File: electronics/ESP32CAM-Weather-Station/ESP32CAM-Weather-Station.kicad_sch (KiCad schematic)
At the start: 93 parts, among them IC1 BME688, IC2 SGP41-D-R4, IC3 VEML7700-TT, IC4 BQ24093DGQR, IC5 BQ29707DSET, IC6 MCP3426A0T-E_SN, IC7 TPS63070RNMR, J1 B4B-PH-SM4-TB_LF__SN_, J10 Conn_01x02_Pin, J2 B4B-PH-SM4-TB_LF__SN_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

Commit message: [WIP] Placed basic 3v3 regulator parts.
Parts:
- Q2: footprint CSD16406Q3:DQG_VSON-CLIP -> DQG_VSON-CLIP
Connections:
- net +3.3V: no longer C5.1
- net +VBAT: no longer S1.1 (NO_1), U2.5 (EN)
- net at Q2.5 (D_1), Q2.6 (D_2), Q2.7 (D_3)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: now also Q2.9 (D_EP), Q3.9 (D_EP)
- net 3V3_PREFUSE: now reaches F2.2, U2.1 (VOUT)
- net 3V3_PREFUSE: now also C5.1
- new net REG_EN: S1.1 (NO_1), U2.5 (EN)
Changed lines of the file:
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@@
 	)
 	(junction
-		(at 349.25 26.67)
-		(diameter 0)
-		(color 0 0 0 0)
-	)
-	(junction
 		(at 40.64 189.23)
 		(diameter 0)
@@
 	)
 	(junction
-		(at 379.73 26.67)
+		(at 137.16 68.58)
 		(diameter 0)
 		(color 0 0 0 0)
 	)
 	(junction
-		(at 137.16 68.58)
+		(at 45.72 142.24)
 		(diameter 0)
 		(color 0 0 0 0)
@@
 	)
 	(junction
+		(at 59.69 58.42)
+		(diameter 0)
+		(color 0 0 0 0)
+	)
+	(junction
 		(at 341.63 241.3)
 		(diameter 0)
@@
 	(wire
 		(pts
+			(xy 59.69 58.42) (xy 72.39 58.42)
+		)
+		(stroke
+			(width 0)
+			(type default)
+		)
+	)
+	(wire
+		(pts
 			(xy 143.51 68.58) (xy 148.59 68.58)
 		)
@@
 	(wire
 		(pts
+			(xy 46.99 58.42) (xy 59.69 58.42)
+		)
+		(stroke
+			(width 0)
+			(type default)
+		)
+	)
+	(wire
+		(pts
 			(xy 341.63 233.68) (xy 347.98 233.68)
 		)
@@
 	(wire
 		(pts
-			(xy 349.25 26.67) (xy 349.25 22.86)
+			(xy 110.49 134.62) (xy 110.49 147.32)
 		)
 		(stroke
@@
 	(wire
 		(pts
-			(xy 349.25 22.86) (xy 379.73 22.86)
+			(xy 71.12 86.36) (xy 76.2 86.36)
 		)
 		(stroke
@@
 	(wire
 		(pts
-			(xy 71.12 86.36) (xy 76.2 86.36)
+			(xy 358.14 236.22) (xy 369.57 236.22)
 		)
 		(stroke
@@
 	(wire
 		(pts
-			(xy 358.14 236.22) (xy 369.57 236.22)
+			(xy 382.27 194.31) (xy 392.43 194.31)
 		)
 		(stroke
@@
 	(wire
 		(pts
-			(xy 382.27 194.31) (xy 392.43 194.31)
+			(xy 45.72 133.35) (xy 45.72 142.24)
 		)
 		(stroke
@@
 	(wire
 		(pts
-			(xy 379.73 22.86) (xy 379.73 26.67)
+			(xy 386.08 157.48) (xy 398.78 157.48)
 		)
 		(stroke
@@
 	(wire
 		(pts
-			(xy 386.08 157.48) (xy 398.78 157.48)
+			(xy 43.18 179.07) (xy 40.64 179.07)
 		)
 		(stroke
@@
 	(wire
 		(pts
-			(xy 43.18 179.07) (xy 40.64 179.07)
+			(xy 342.9 160.02) (xy 355.6 160.02)
 		)
 		(stroke
@@
 	(wire
 		(pts
-			(xy 342.9 160.02) (xy 355.6 160.02)
+			(xy 274.32 190.5) (xy 273.05 190.5)
 		)
 		(stroke
@@
 	(wire
 		(pts
-			(xy 274.32 190.5) (xy 273.05 190.5)
+			(xy 73.66 147.32) (xy 82.55 147.32)
 		)
 		(stroke
@@
 	(wire
 		(pts
-			(xy 73.66 147.32) (xy 82.55 147.32)
+			(xy 106.68 269.24) (xy 116.84 269.24)
 		)
 		(stroke
@@
 	(wire
 		(pts
-			(xy 106.68 269.24) (xy 116.84 269.24)
+			(xy 59.69 58.42) (xy 59.69 53.34)
 		)
 		(stroke
@@
 		)
 	)
+	(label "3V3_PREFUSE"
+		(at 110.49 134.62 180)
+		(effects
+			(font
+				(size 1.27 1.27)
+			)
+			(justify right bottom)
+		)
+	)
 	(label "5V_REG_PG"
 		(at 163.83 55.88 180)
@@
 		)
 	)
+	(label "3V3_PREFUSE"
+		(at 45.72 133.35 0)
+		(effects
+			(font
+				(size 1.27 1.27)
+			)
+			(justify left bottom)
+		)
+	)
 	(label "5V_REG_VAUX"
 		(at 137.16 30.48 180)
@@
 		(pin "4"
 		)
+		(pin "9"
+		)
 		(instances
 			(project "ESP32CAM-Weather-Station"
@@
 	)
 	(symbol
-		(lib_id "power:+3.3V")
-		(at 110.49 147.32 0)
-		(unit 1)
-		(exclude_from_sim no)
-		(in_bom yes)
-		(on_board yes)
-		(dnp no)
-		(fields_autoplaced yes)
-		(property "Reference" "#PWR054"
-			(at 110.49 151.13 0)
-			(effects
-				(font
-					(size 1.27 1.27)
-				)
-				(hide yes)
-			)
-		)
-		(property "Value" "+3.3V"
-			(at 110.49 142.24 0)
-			(effects
-				(font
-					(size 1.27 1.27)
-				)
-			)
-		)
-		(property "Footprint" ""
-			(at 110.49 147.32 0)
-			(effects
-				(font
-					(size 1.27 1.27)
-				)
-				(hide yes)
-			)
-		)
-		(property "Datasheet" ""
-			(at 110.49 147.32 0)
-			(effects
-				(font
-					(size 1.27 1.27)
-				)
-				(hide yes)
-			)
-		)
-		(property "Description" "Power symbol creates a global label with name \"+3.3V\""
-			(at 110.49 147.32 0)
-			(effects
-				(font
-					(size 1.27 1.27)
-				)
-				(hide yes)
-			)
-		)
-		(pin "1"
-		)
-		(instances
-			(project "ESP32CAM-Weather-Station"
-				(path "/7d0fd3b7-d6b0-4ab6-a180-9a1d35f36f7a"
-					(reference "#PWR054")
-					(unit 1)
-				)
-			)
-		)
-	)
-	(symbol
 		(lib_id "power:GND")
 		(at 161.29 237.49 0)
@@
 	)
 	(symbol
+		(lib_name "CSD16406Q3_1")
 		(lib_id "CSD16406Q3:CSD16406Q3")
 		(at 34.29 45.72 0)
@@
 			)
 		)
-		(property "Footprint" "CSD16406Q3:DQG_VSON-CLIP"
+		(property "Footprint" "DQG_VSON-CLIP"
 			(at 55.88 43.18 0)
 			(effects
@@
 		(pin "4"
 		)
+		(pin "9"
+		)
 		(instances

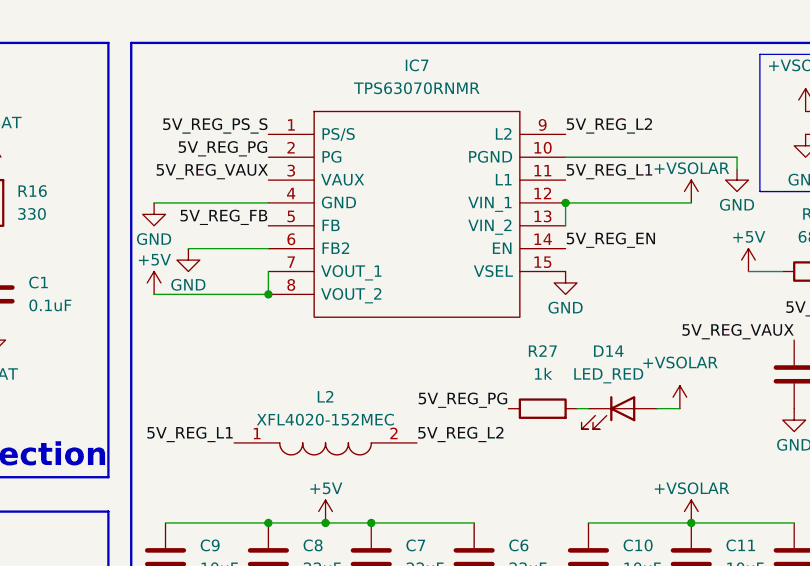
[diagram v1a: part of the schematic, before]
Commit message: [WIP] Placed basic 5V regulator parts and moved 3V3 regulator so that output connects to the 3V3 plane.
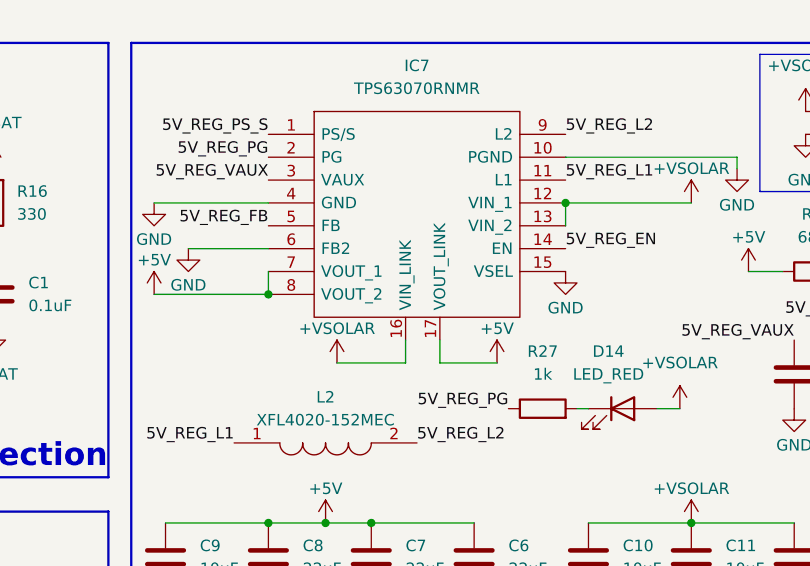
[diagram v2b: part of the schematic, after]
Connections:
- net +5V: now also IC7.17 (VOUT_LINK)
- net +VSOLAR: now also IC7.16 (VIN_LINK)
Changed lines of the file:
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@@
 	(wire
 		(pts
+			(xy 162.56 50.8) (xy 156.21 50.8)
+		)
+		(stroke
+			(width 0)
+			(type default)
+		)
+	)
+	(wire
+		(pts
 			(xy 184.15 68.58) (xy 195.58 68.58)
 		)
@@
 	(wire
 		(pts
+			(xy 144.78 50.8) (xy 152.4 50.8)
+		)
+		(stroke
+			(width 0)
+			(type default)
+		)
+	)
+	(wire
+		(pts
+			(xy 152.4 50.8) (xy 152.4 48.26)
+		)
+		(stroke
+			(width 0)
+			(type default)
+		)
+	)
+	(wire
+		(pts
 			(xy 60.96 269.24) (xy 71.12 269.24)
 		)
@@
 	(wire
 		(pts
+			(xy 156.21 50.8) (xy 156.21 48.26)
+		)
+		(stroke
+			(width 0)
+			(type default)
+		)
+	)
+	(wire
+		(pts
 			(xy 85.09 41.91) (xy 39.37 41.91)
 		)
@@
 	)
 	(symbol
+		(lib_id "power:+BATT")
+		(at 144.78 50.8 0)
+		(unit 1)
+		(exclude_from_sim no)
+		(in_bom yes)
+		(on_board yes)
+		(dnp no)
+		(property "Reference" "#PWR013"
+			(at 144.78 54.61 0)
+			(effects
+				(font
+					(size 1.27 1.27)
+				)
+				(hide yes)
+			)
+		)
+		(property "Value" "+VSOLAR"
+			(at 144.78 46.99 0)
+			(effects
+				(font
+					(size 1.27 1.27)
+				)
+			)
+		)
+		(property "Footprint" ""
+			(at 144.78 50.8 0)
+			(effects
+				(font
+					(size 1.27 1.27)
+				)
+				(hide yes)
+			)
+		)
+		(property "Datasheet" ""
+			(at 144.78 50.8 0)
+			(effects
+				(font
+					(size 1.27 1.27)
+				)
+				(hide yes)
+			)
+		)
+		(property "Description" "Power symbol creates a global label with name \"+BATT\""
+			(at 144.78 50.8 0)
+			(effects
+				(font
+					(size 1.27 1.27)
+				)
+				(hide yes)
+			)
+		)
+		(pin "1"
+		)
+		(instances
+			(project "ESP32CAM-Weather-Station"
+				(path "/7d0fd3b7-d6b0-4ab6-a180-9a1d35f36f7a"
+					(reference "#PWR013")
+					(unit 1)
+				)
+			)
+		)
+	)
+	(symbol
 		(lib_id "power:GND")
 		(at 382.27 196.85 0)
@@
 	)
 	(symbol
+		(lib_id "power:+5V")
+		(at 162.56 50.8 0)
+		(unit 1)
+		(exclude_from_sim no)
+		(in_bom yes)
+		(on_board yes)
+		(dnp no)
+		(property "Reference" "#PWR014"
+			(at 162.56 54.61 0)
+			(effects
+				(font
+					(size 1.27 1.27)
+				)
+				(hide yes)
+			)
+		)
+		(property "Value" "+5V"
+			(at 162.56 46.99 0)
+			(effects
+				(font
+					(size 1.27 1.27)
+				)
+			)
+		)
+		(property "Footprint" ""
+			(at 162.56 50.8 0)
+			(effects
+				(font
+					(size 1.27 1.27)
+				)
+				(hide yes)
+			)
+		)
+		(property "Datasheet" ""
+			(at 162.56 50.8 0)
+			(effects
+				(font
+					(size 1.27 1.27)
+				)
+				(hide yes)
+			)
+		)
+		(property "Description" "Power symbol creates a global label with name \"+5V\""
+			(at 162.56 50.8 0)
+			(effects
+				(font
+					(size 1.27 1.27)
+				)
+				(hide yes)
+			)
+		)
+		(pin "1"
+		)
+		(instances
+			(project "ESP32CAM-Weather-Station"
+				(path "/7d0fd3b7-d6b0-4ab6-a180-9a1d35f36f7a"
+					(reference "#PWR014")
+					(unit 1)
+				)
+			)
+		)
+	)
+	(symbol
 		(lib_id "power:+3.3V")
 		(at 274.32 190.5 0)
@@
 		(pin "1"
 		)
+		(pin "16"
+		)
+		(pin "17"
+		)
 		(instances
